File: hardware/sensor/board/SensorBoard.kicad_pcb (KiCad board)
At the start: 4 copper layers, 40 x 25 mm, 36 parts, among them J1 USB_B_Mini, J2 Conn_01x04_Male, U1 93LC56BT-I/OT, U2 FT232H, U3 74LVC2G17, U4 74LVC1G374, U5 74LVC1G04, Y1 12MHz

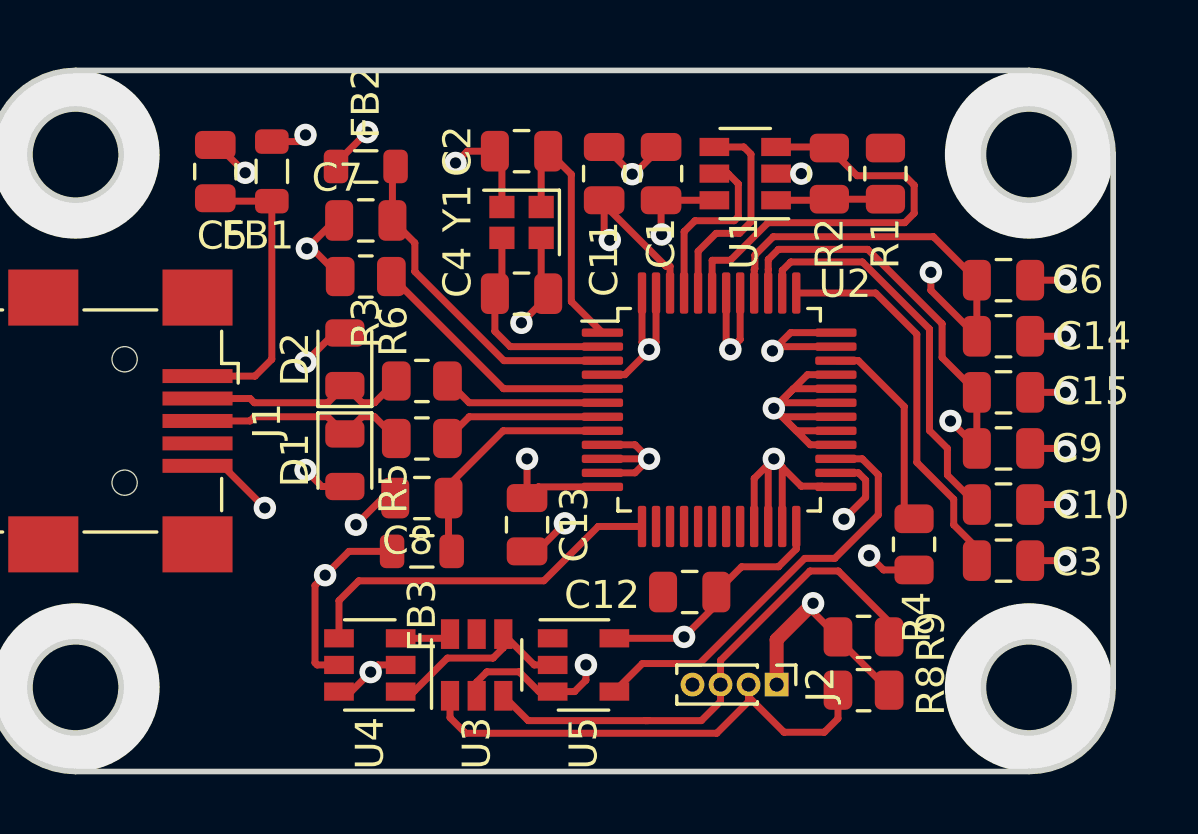
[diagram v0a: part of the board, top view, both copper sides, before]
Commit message: 0603 Component attempt 1
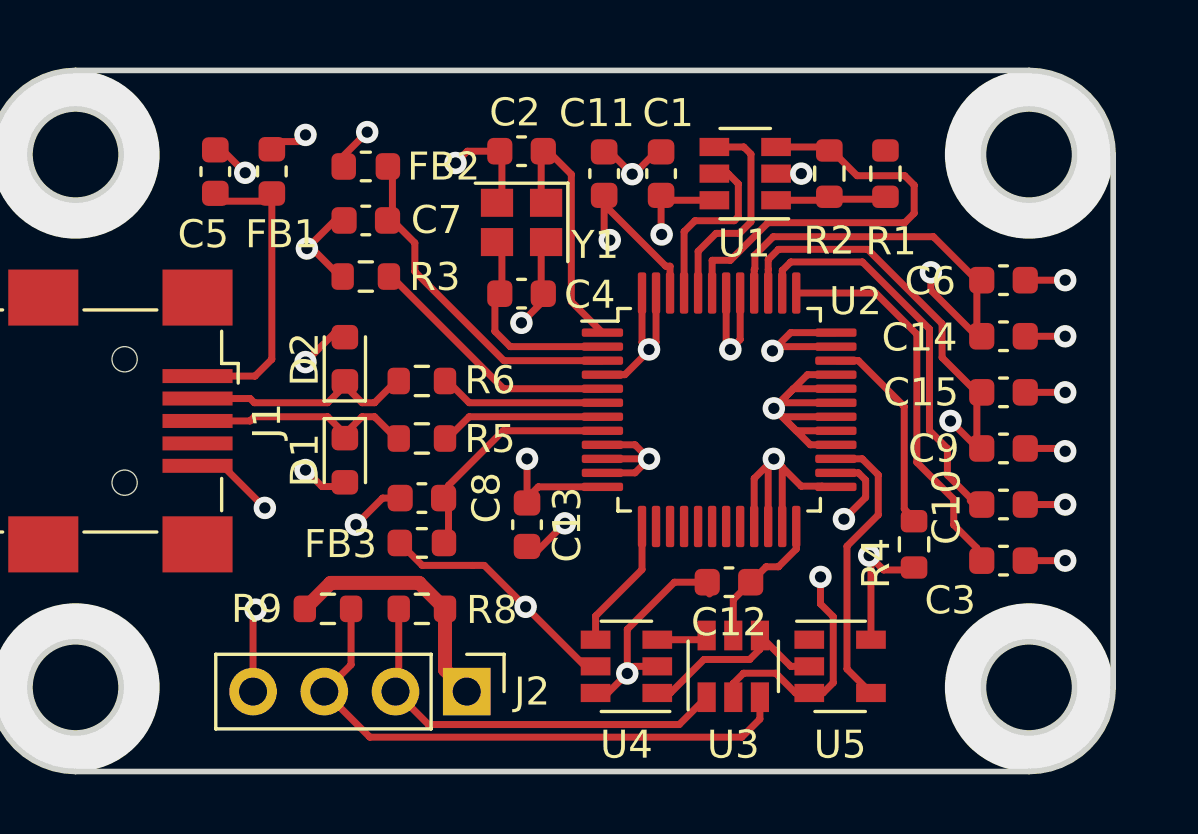
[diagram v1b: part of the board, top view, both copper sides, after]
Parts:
- C1, C3: value .1uF -> 0.1uF; footprint Capacitor_SMD:C_0805_2012Metric -> Capacitor_SMD:C_0603_1608Metric
- C10, C11, C12, C13, C14, C15, C2, C4, C5, C6, C7, C8, C9: footprint Capacitor_SMD:C_0805_2012Metric -> Capacitor_SMD:C_0603_1608Metric
- D1, D2: footprint Diode_SMD:D_0805_2012Metric -> Diode_SMD:D_0603_1608Metric
- FB1, FB2, FB3: footprint Inductor_SMD:L_0805_2012Metric -> Inductor_SMD:L_0603_1608Metric
- J2: footprint Connector_PinHeader_1.00mm:PinHeader_1x04_P1.00mm_Vertical -> Connector_PinHeader_2.54mm:PinHeader_1x04_P2.54mm_Vertical
- R1, R2, R3, R4, R5, R6, R8, R9: footprint Resistor_SMD:R_0805_2012Metric -> Resistor_SMD:R_0603_1608Metric
- Y1: footprint Crystal:Crystal_SMD_2016-4Pin_2.0x1.6mm -> Crystal:Crystal_SMD_2520-4Pin_2.5x2.0mm
- moved R9 19.1 mm to (12.0, 19.2)
- moved R8 16.0 mm to (15.3, 19.2)
- moved J2 11.1 mm to (16.9, 22.1)
- moved U3 9.15 mm to (26.5, 21.2)
- moved U4 9.15 mm to (22.6, 21.2)
- moved U5 9.15 mm to (30.3, 21.2)
- moved C12 1.44 mm to (26.3, 18.2)
- moved FB3 0.30 mm to (15.3, 16.9)
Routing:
- net GND: track 87.9 -> 99.1 mm, vias 25 -> 26
- net DIR: track 13.2 -> 4.72 mm
- net WR#: track 15.2 -> 10.3 mm
- net Net-(J2-Pad2): track 18.1 -> 15.0 mm
- net Net-(J2-Pad3): track 18.7 -> 20.6 mm
- net VBUS: track 63.4 -> 64.7 mm, vias 3 -> 2
- net VCC3V3: track 116.4 -> 117.6 mm, vias 9 -> 8
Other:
- rule pad_to_mask_clearance: 0 -> 0.0508
- rule trace_min: 0.2 -> 0.127
- rule via_min_drill: 0.3 -> 0.254
- rule via_min_size: 0.4 -> 0.4572

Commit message: Layout from scratch
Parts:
- added D3: LED, LED_SMD:LED_0603_1608Metric, F.Cu at (120.5, 93.1)
- added R7: 1k, Resistor_SMD:R_0603_1608Metric, F.Cu at (123.6, 93.1)
- moved R9 139.8 mm to (133.7, 88.0), turned to 270 degrees
- moved R8 135.1 mm to (133.7, 84.5), turned to 270 degrees
- moved J2 134.2 mm to (136.2, 83.7), turned to 0 degrees
- moved C1 127.9 mm to (127.2, 79.2)
- moved U1 127.8 mm to (129.8, 79.5)
- moved R2 127.7 mm to (132.5, 79.6)
- moved U3 127.0 mm to (129.2, 95.8), turned to 180 degrees
- moved R1 127.0 mm to (131.8, 82.0), turned to 180 degrees
- moved R3 126.8 mm to (113.7, 84.8)
- moved C5 126.5 mm to (110.0, 78.4)
- moved FB2 126.2 mm to (112.3, 81.8)
- moved FB1 126.1 mm to (111.5, 78.4)
- moved C7 125.9 mm to (112.3, 83.3)
- moved J1 125.5 mm to (105.4, 87.5)
- moved C2 125.1 mm to (117.8, 79.5), turned to 270 degrees
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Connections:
- net Net-(C2-Pad1) renamed /CLK+
- net Net-(C3-Pad1) renamed /VCCA
- net Net-(C4-Pad1) renamed /CLK-
- net Net-(J2-Pad2) renamed /Phase1
- net Net-(J2-Pad3) renamed /Phase2
- net Net-(R3-Pad1) renamed /REF
- net Net-(R4-Pad1) renamed /RESET
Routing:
- net Net-(J1-Pad6): track 0.00 -> 19.8 mm
- net GND: track 99.1 -> 79.8 mm, vias 26 -> 27
- net VBUS: track 64.7 -> 46.6 mm, vias 2 -> 3
- net /Phase2: track 20.6 -> 10.1 mm
- net EECS: track 6.52 -> 16.3 mm
- net Net-(U3-Pad6): track 1.82 -> 9.16 mm
- net VCC3V3: track 117.6 -> 111.2 mm, vias 8 -> 10
- net VPHY: track 12.1 -> 6.32 mm
- net /REF: track 9.18 -> 3.38 mm
- net Net-(U3-Pad4): track 7.01 -> 12.8 mm
- net EECLK: track 7.63 -> 13.0 mm
- net /Phase1: track 15.0 -> 18.6 mm
- net VCORE: track 14.4 -> 10.9 mm
- net D+: track 5.88 -> 2.79 mm
- net D-: track 5.88 -> 2.79 mm
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- added copper zone on B.Cu, net GND
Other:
- net class Default: clearance 0.2 -> 0.127
- net class USB removed
- rule trace_clearance: 0.2 -> 0.127

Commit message: Update SensorBoard.kicad_pcb
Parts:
- moved U4 5.25 mm to (113.5, 95.8)
- moved U5 5.25 mm to (118.7, 95.8)
- moved WR# 4.79 mm to (123.5, 96.9)
- moved C12 3.93 mm to (122.9, 93.2), turned to 180 degrees
- moved R7 3.61 mm to (126.0, 95.8), turned to 270 degrees
- moved U3 1.55 mm to (130.8, 95.8)
- renumbered J2 to +, U2 to UM232H, D3 to WR#
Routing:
- net VCC3V3: track 111.2 -> 48.4 mm
- net VBUS: track 46.6 -> 20.1 mm
- net Net-(U3-Pad4): track 12.8 -> 19.6 mm
- net Net-(U3-Pad6): track 9.16 -> 16.0 mm
- net WR#: track 9.10 -> 14.0 mm
- net GND: track 79.8 -> 83.4 mm
- net DIR: track 4.69 -> 7.33 mm
- net /Phase1: track 18.6 -> 17.0 mm
- net /Phase2: track 10.1 -> 9.37 mm
- added copper zone on In1.Cu, net GND
- added copper zone on B.Cu, net VBUS
- added copper zone on In2.Cu, net VCC3V3
- removed copper zone on B.Cu, net GND
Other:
- board text added: "v0.4"

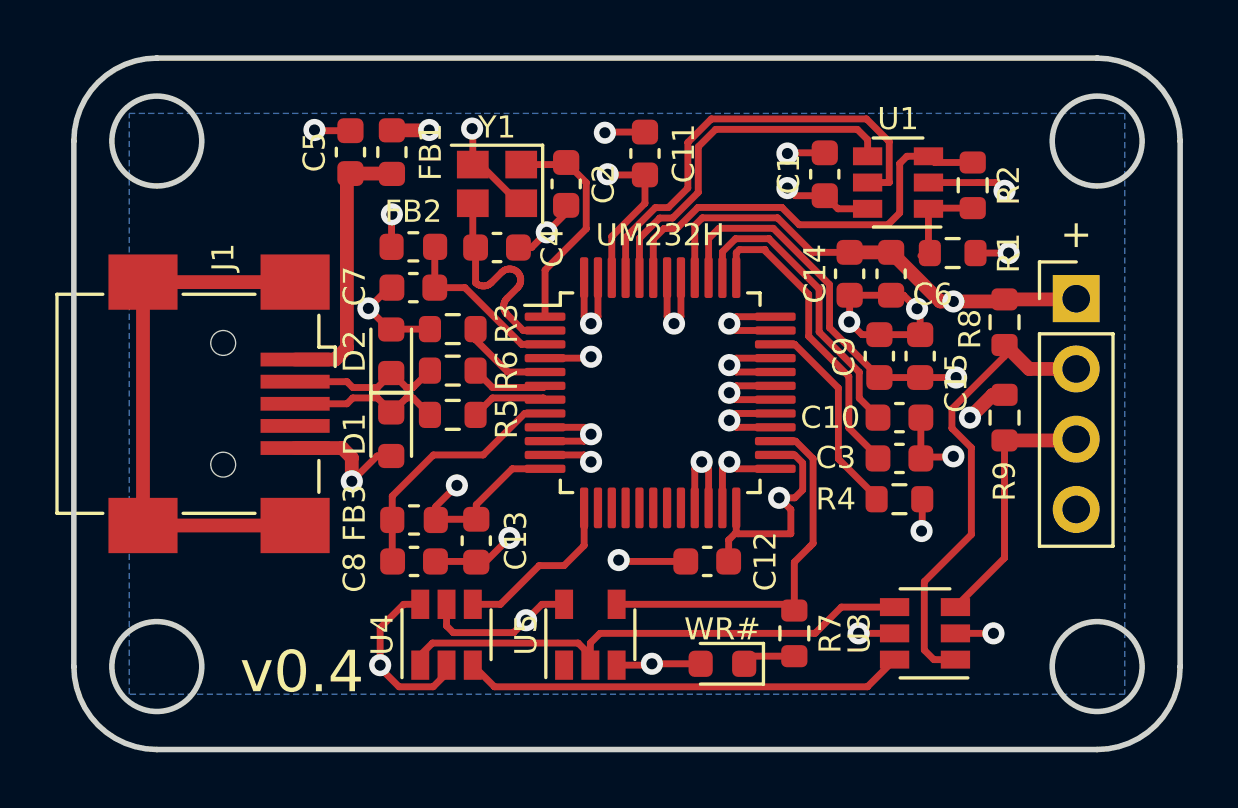
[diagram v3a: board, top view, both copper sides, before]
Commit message: Rev 0.5
Added power planes galore, put bypass caps closer to UM232H
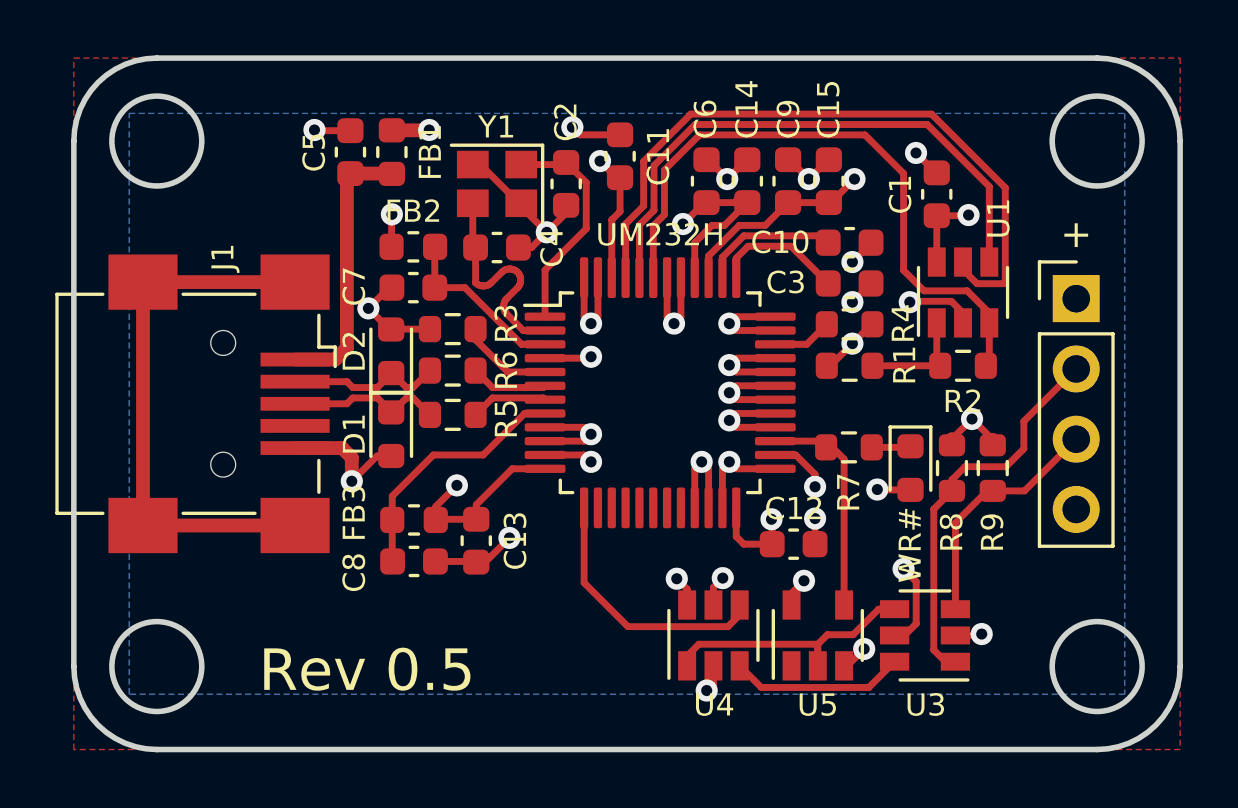
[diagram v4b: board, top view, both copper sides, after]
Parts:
- moved WR# 9.81 mm to (130.2, 89.8), turned to 270 degrees
- moved U4 9.65 mm to (123.1, 95.9)
- moved U5 8.23 mm to (126.9, 95.9)
- moved C6 7.47 mm to (122.9, 79.5), turned to 90 degrees
- moved C15 7.13 mm to (127.3, 79.5)
- moved C9 7.13 mm to (125.8, 79.5)
- moved R7 7.01 mm to (128.0, 89.1), turned to 0 degrees
- moved C10 6.58 mm to (128.1, 81.7)
- moved R4 6.58 mm to (128.1, 84.6)
- moved C3 6.58 mm to (128.1, 83.2)
- moved R2 6.53 mm to (132.2, 86.1), turned to 180 degrees
- moved R8 5.61 mm to (131.8, 89.8)
- moved R1 5.52 mm to (128.1, 86.1), turned to 0 degrees
- moved C14 4.99 mm to (124.3, 79.5), turned to 90 degrees
- moved U1 4.62 mm to (132.2, 83.5), turned to 90 degrees
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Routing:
- net VCC3V3: track 48.4 -> 35.8 mm, vias 10 -> 11
- net GND: track 83.4 -> 72.7 mm, vias 27 -> 29
- net Net-(U3-Pad4): track 19.6 -> 9.34 mm
- net Net-(U3-Pad6): track 16.0 -> 6.31 mm
- net VBUS: track 20.1 -> 10.4 mm
- net EECS: track 16.3 -> 24.8 mm
- net EECLK: track 13.0 -> 20.7 mm
- net EEDATA: track 15.8 -> 23.0 mm
- net /VCCA: track 11.2 -> 4.76 mm
- net WR#: track 14.0 -> 8.03 mm
- net VCORE: track 10.9 -> 4.99 mm
- net /RESET: track 7.45 -> 2.16 mm
- net /Phase1: track 17.0 -> 14.1 mm
- net DIR: track 7.33 -> 10.2 mm
- net /Phase2: track 9.37 -> 8.81 mm
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- added copper zone on F.Cu, net GND
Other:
- board text added: "Rev 0.5"
- board text removed: "v0.4"

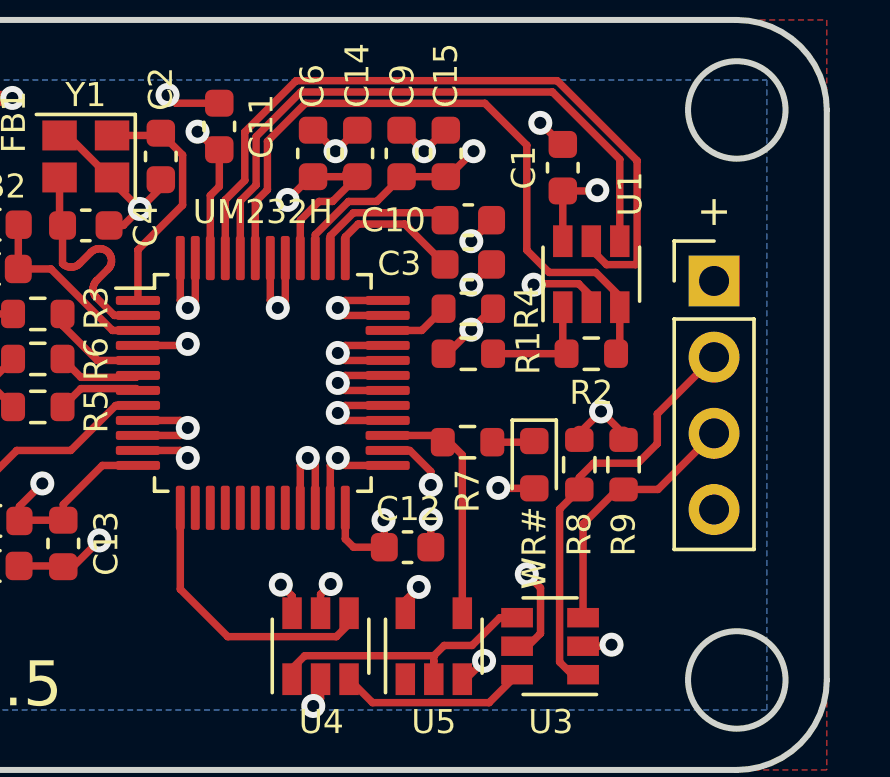
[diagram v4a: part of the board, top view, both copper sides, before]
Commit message: Rev 0.5
Added a debug LED, changed to crosshair reliefs on layer 1 ground plane
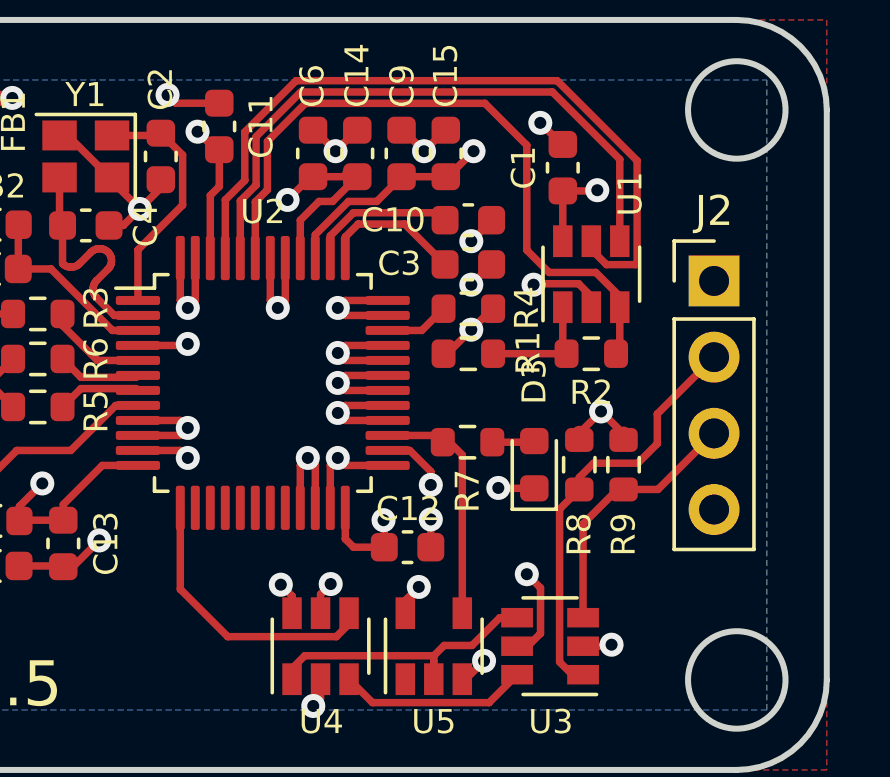
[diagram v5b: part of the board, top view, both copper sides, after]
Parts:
- turned D3 to 90 degrees
- renumbered WR# to D3, + to J2, UM232H to U2
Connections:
- D3 pad 1: Net-(D3-Pad1) -> GND
- D3 pad 2: GND -> Net-(D3-Pad2)
- R7 pad 2: Net-(D3-Pad1) -> Net-(D3-Pad2)
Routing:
- net Net-(D3-Pad2): track 0.00 -> 1.39 mm
- net Net-(D3-Pad1): track 1.39 -> 0.00 mm
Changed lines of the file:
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@@
     (33 F.Adhes user hide)
     (34 B.Paste user hide)
-    (35 F.Paste user hide)
+    (35 F.Paste user)
     (36 B.SilkS user hide)
     (37 F.SilkS user)
@@
     (40 Dwgs.User user hide)
     (41 Cmts.User user hide)
-    (42 Eco1.User user hide)
+    (42 Eco1.User user)
     (43 Eco2.User user hide)
     (44 Edge.Cuts user)
@@
       (outputformat 1)
       (mirror false)
-      (drillshape 1)
+      (drillshape 0)
       (scaleselection 1)
-      (outputdirectory ""))
+      (outputdirectory "plots/"))
   )
   (net 0 "")
@@
   (net 34 /Phase2)
   (net 35 /Phase1)
-  (net 36 "Net-(D3-Pad1)")
+  (net 36 "Net-(D3-Pad2)")
   (net_class Default "This is the default net class."
     (clearance 0.127)
@@
     (add_net GND)
     (add_net "Net-(C5-Pad1)")
-    (add_net "Net-(D3-Pad1)")
+    (add_net "Net-(D3-Pad2)")
     (add_net "Net-(J1-Pad4)")
     (add_net "Net-(J1-Pad6)")
@@
     (fp_line (start 1.48 0.73) (end -1.48 0.73) (layer F.CrtYd) (width 0.05))
     (pad 2 smd roundrect (at 0.825 0) (size 0.8 0.95) (layers F.Cu F.Paste F.Mask) (roundrect_rratio 0.25)
-      (net 36 "Net-(D3-Pad1)"))
+      (net 36 "Net-(D3-Pad2)"))
     (pad 1 smd roundrect (at -0.825 0) (size 0.8 0.95) (layers F.Cu F.Paste F.Mask) (roundrect_rratio 0.25)
       (net 16 WR#))
@@
   )
   (module LED_SMD:LED_0603_1608Metric (layer F.Cu)
-    (at 130.25 89.825 270)
+    (at 130.25 89.825 90)
     (descr "LED SMD 0603 (1608 Metric), square (rectangular) end terminal, IPC_7351 nominal, (Body size source: http://www.tortai-tech.com/upload/download/2011102023233369053.pdf), generated with kicad-footprint-generator")
     (tags LED)
     (attr smd)
-    (fp_text reference WR# (at 2.775 0 90) (layer F.SilkS)
+    (fp_text reference D3 (at 2.775 0 90) (layer F.SilkS)
       (effects (font (size 0.8 0.8) (thickness 0.125)))
     )
@@
     (fp_line (start 1.48 -0.73) (end 1.48 0.73) (layer F.CrtYd) (width 0.05))
     (fp_line (start 1.48 0.73) (end -1.48 0.73) (layer F.CrtYd) (width 0.05))
-    (pad 2 smd roundrect (at 0.7875 0 270) (size 0.875 0.95) (layers F.Cu F.Paste F.Mask) (roundrect_rratio 0.25)
-      (net 1 GND))
-    (pad 1 smd roundrect (at -0.7875 0 270) (size 0.875 0.95) (layers F.Cu F.Paste F.Mask) (roundrect_rratio 0.25)
-      (net 36 "Net-(D3-Pad1)"))
+    (pad 2 smd roundrect (at 0.7875 0 90) (size 0.875 0.95) (layers F.Cu F.Paste F.Mask) (roundrect_rratio 0.25)
+      (net 36 "Net-(D3-Pad2)"))
+    (pad 1 smd roundrect (at -0.7875 0 90) (size 0.875 0.95) (layers F.Cu F.Paste F.Mask) (roundrect_rratio 0.25)
+      (net 1 GND))
     (model ${KISYS3DMOD}/LED_SMD.3dshapes/LED_0603_1608Metric.wrl
       (at (xyz 0 0 0))
@@
     (tags "LQFP QFP")
     (attr smd)
-    (fp_text reference UM232H (at 0 -5.7 180) (layer F.SilkS)
+    (fp_text reference U2 (at 0 -5.7 180) (layer F.SilkS)
       (effects (font (size 0.8 0.8) (thickness 0.125)))
     )
@@
     (descr "Through hole straight pin header, 1x04, 2.54mm pitch, single row")
     (tags "Through hole pin header THT 1x04 2.54mm single row")
-    (fp_text reference + (at 0 -2.33) (layer F.SilkS)
+    (fp_text reference J2 (at 0 -2.33) (layer F.SilkS)
       (effects (font (size 1 1) (thickness 0.15)))
     )
@@
   )
   (zone (net 1) (net_name GND) (layer F.Cu) (hatch edge 0.508)
-    (connect_pads thru_hole_only (clearance 0.254))
+    (connect_pads (clearance 0.254))
     (min_thickness 0.254)
     (fill yes (arc_segments 32) (thermal_gap 0.508) (thermal_bridge_width 0.508) (smoothing fillet))
